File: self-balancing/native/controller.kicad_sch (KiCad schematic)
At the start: 13 parts, among them U1 STM32H743VIT6

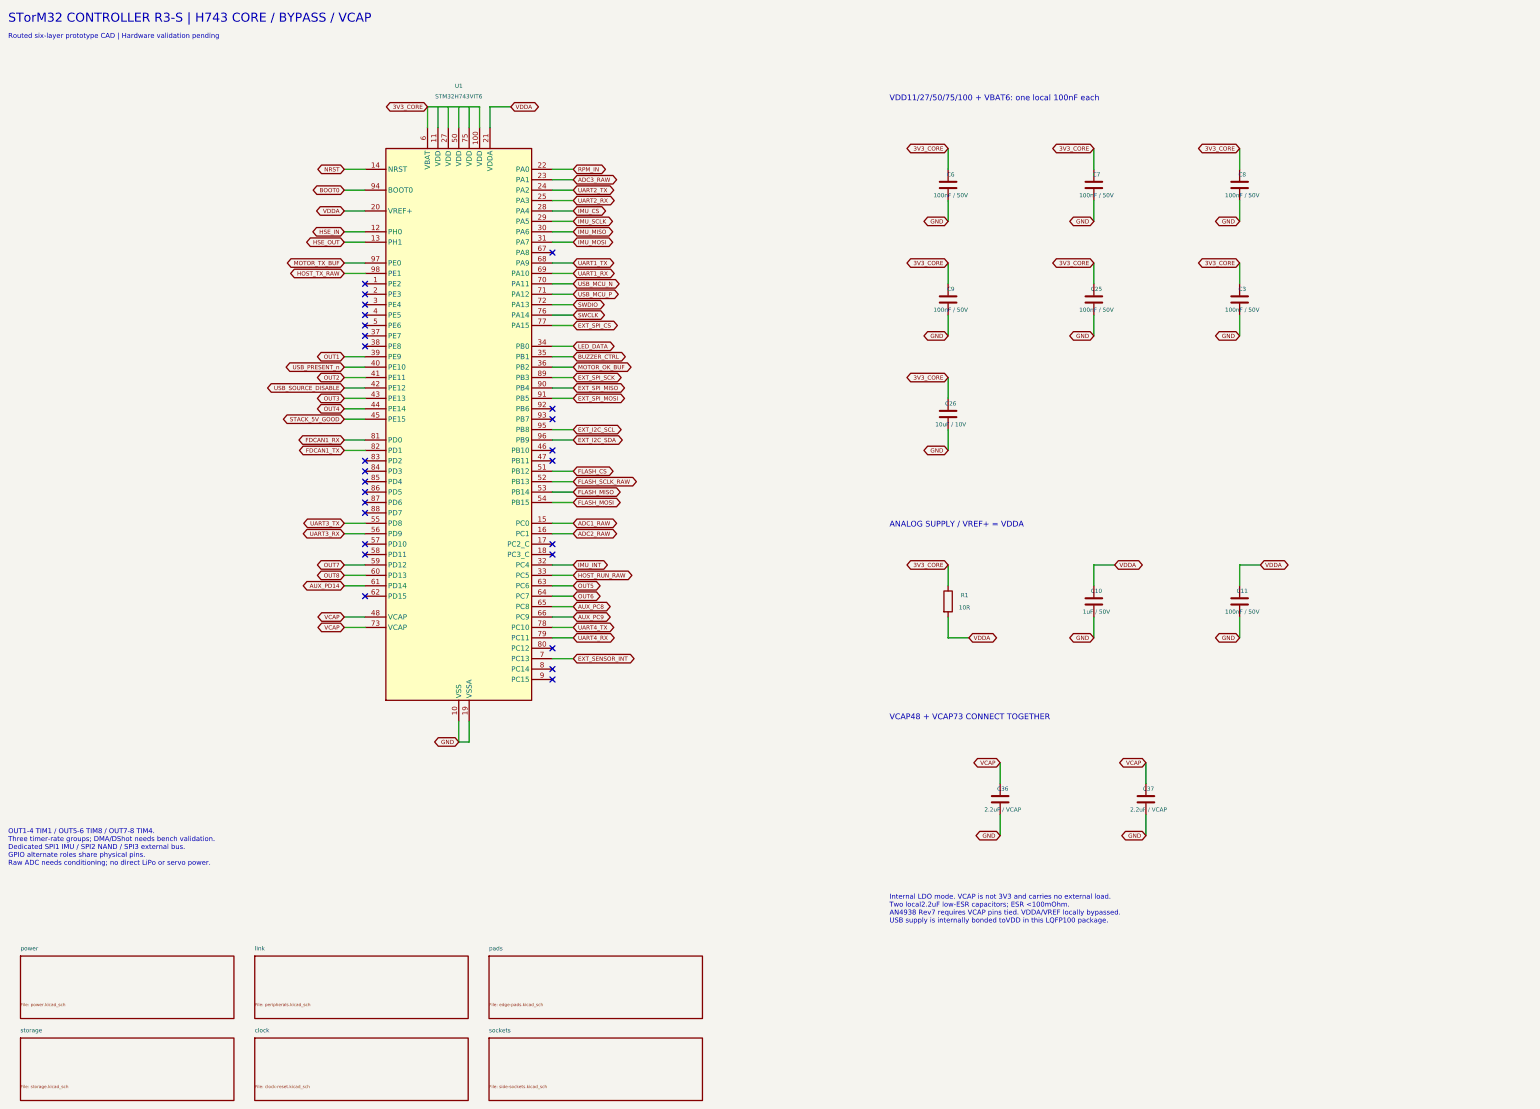
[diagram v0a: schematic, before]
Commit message: Improve H743 schematic readability with wired functional groups
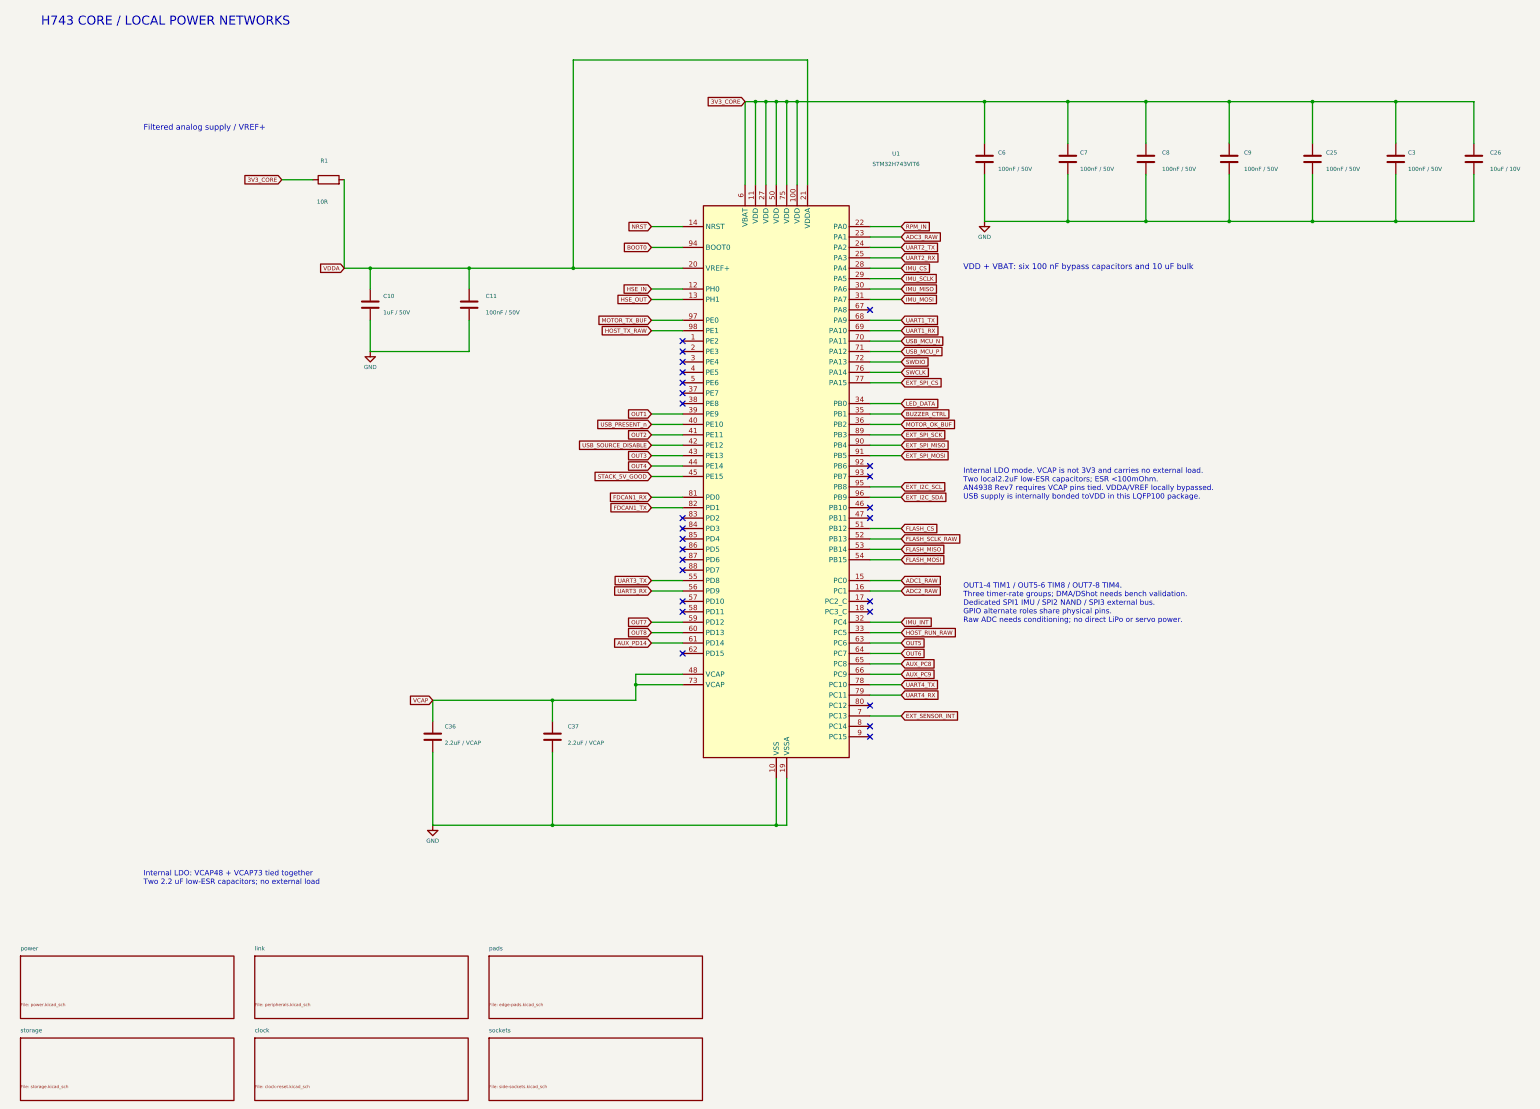
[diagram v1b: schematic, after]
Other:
- note added: "Filtered analog supply / VREF+"
- note added: "H743 CORE / LOCAL POWER NETWORKS"
- note added: "Internal LDO: VCAP48 + VCAP73 tied together Two 2.2 uF low-ESR capacitors; no external load"
- note added: "VDD + VBAT: six 100 nF bypass capacitors and 10 uF bulk"
- note removed: "ANALOG SUPPLY / VREF+ = VDDA"
- note removed: "Routed six-layer prototype CAD | Hardware validation pending"
- note removed: "STorM32 CONTROLLER R3-S | H743 CORE / BYPASS / VCAP"
- note removed: "VCAP48 + VCAP73 CONNECT TOGETHER"
- note removed: "VDD11/27/50/75/100 + VBAT6: one local 100nF each"
- moved on the sheet: C10, C11, C25, C26, C3, C36, C37, C6, C7, C8, C9, R1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
